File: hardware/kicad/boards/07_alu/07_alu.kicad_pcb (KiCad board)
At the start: 2 copper layers, 99.8 x 99.7 mm, 185 parts, among them J10 Conn_01x04_Pin, J11 Conn_01x04_Pin, J12 Conn_01x08_Pin, J15 Conn_01x08_Pin, J16 Conn_01x08_Pin, J17 Conn_01x08_Pin, J5 Conn_01x08_Pin, J6 Conn_01x08_Pin, J7 Conn_01x08_Pin, U16 74ACT151, U3 74ACT283, U36 74HC86, U37 74LS08, U38 74LS540, U4 74HC688, U40 74LS377, U41 74ACT151, U42 74ACT151, U43 74ACT151, U44 74ACT151, U45 74ACT151, U46 74ACT151, U47 74ACT151, U48 74ACT151, U49 74ACT151, U5 74ACT283, U50 74ACT151, U51 74ACT151, U52 74ACT151, U53 74ACT151, U54 74ACT151, U55 74ACT151, U56 74ACT151

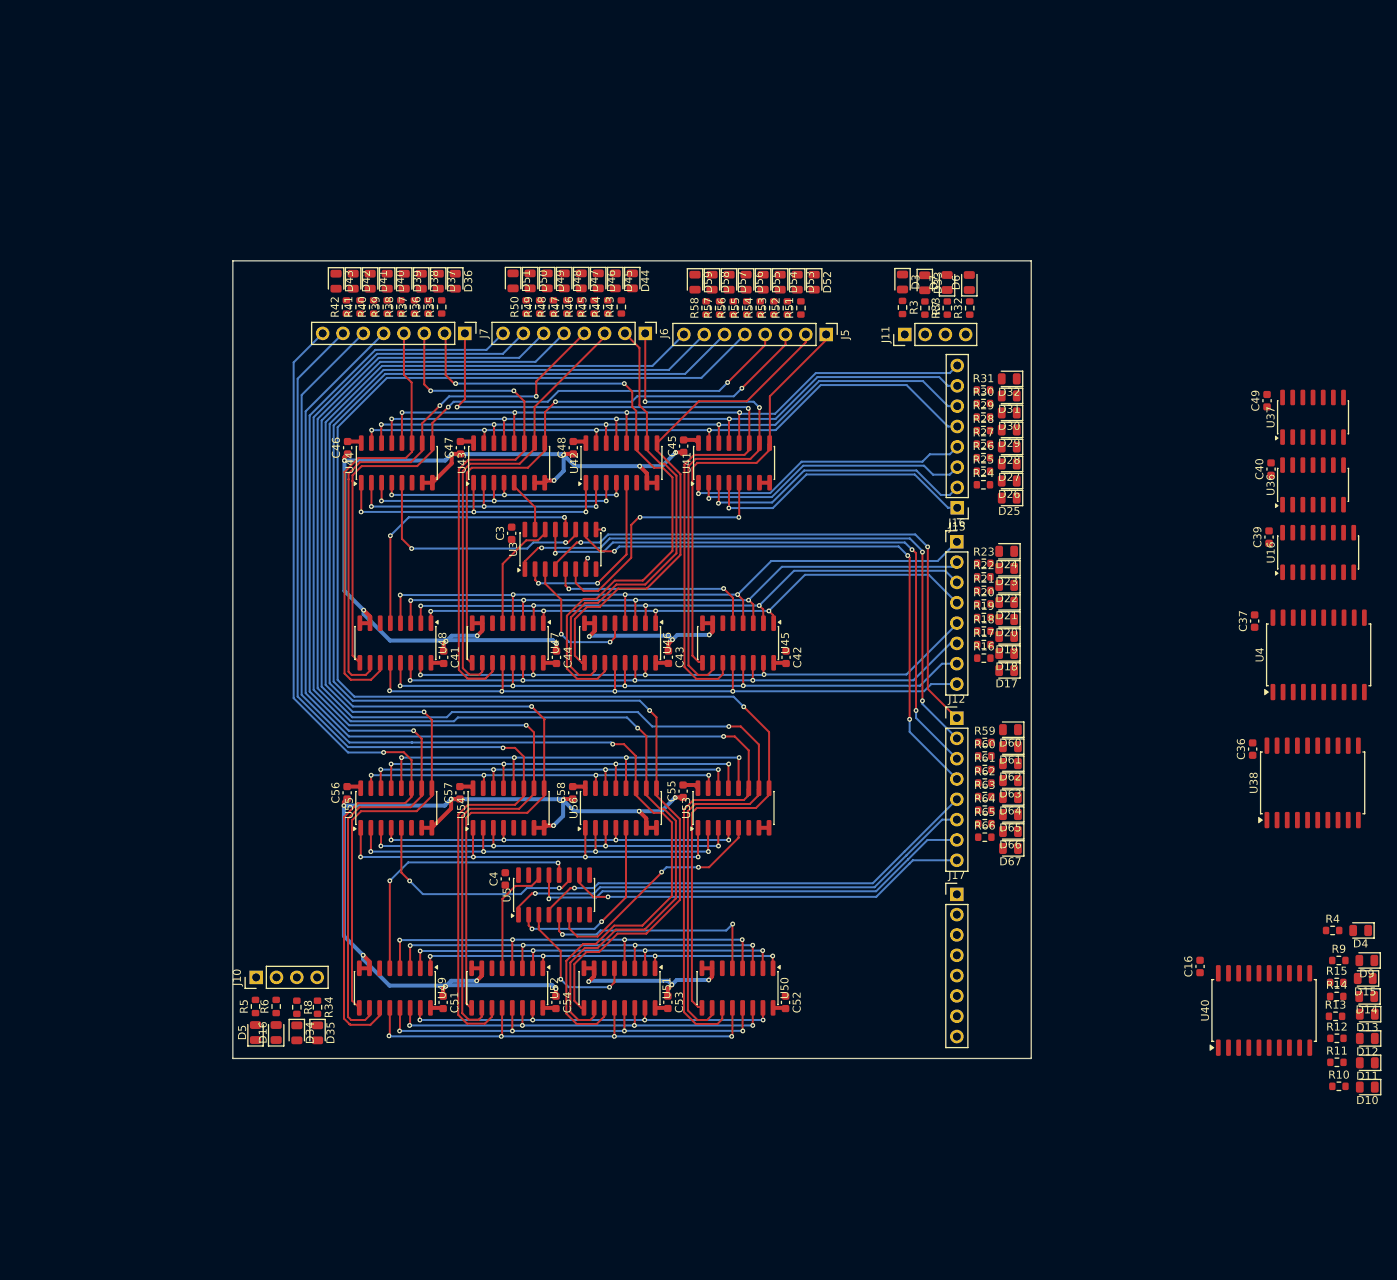
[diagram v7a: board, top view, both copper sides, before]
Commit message: checkpoint: routing flags and finishing final traces before pcb annotations and text
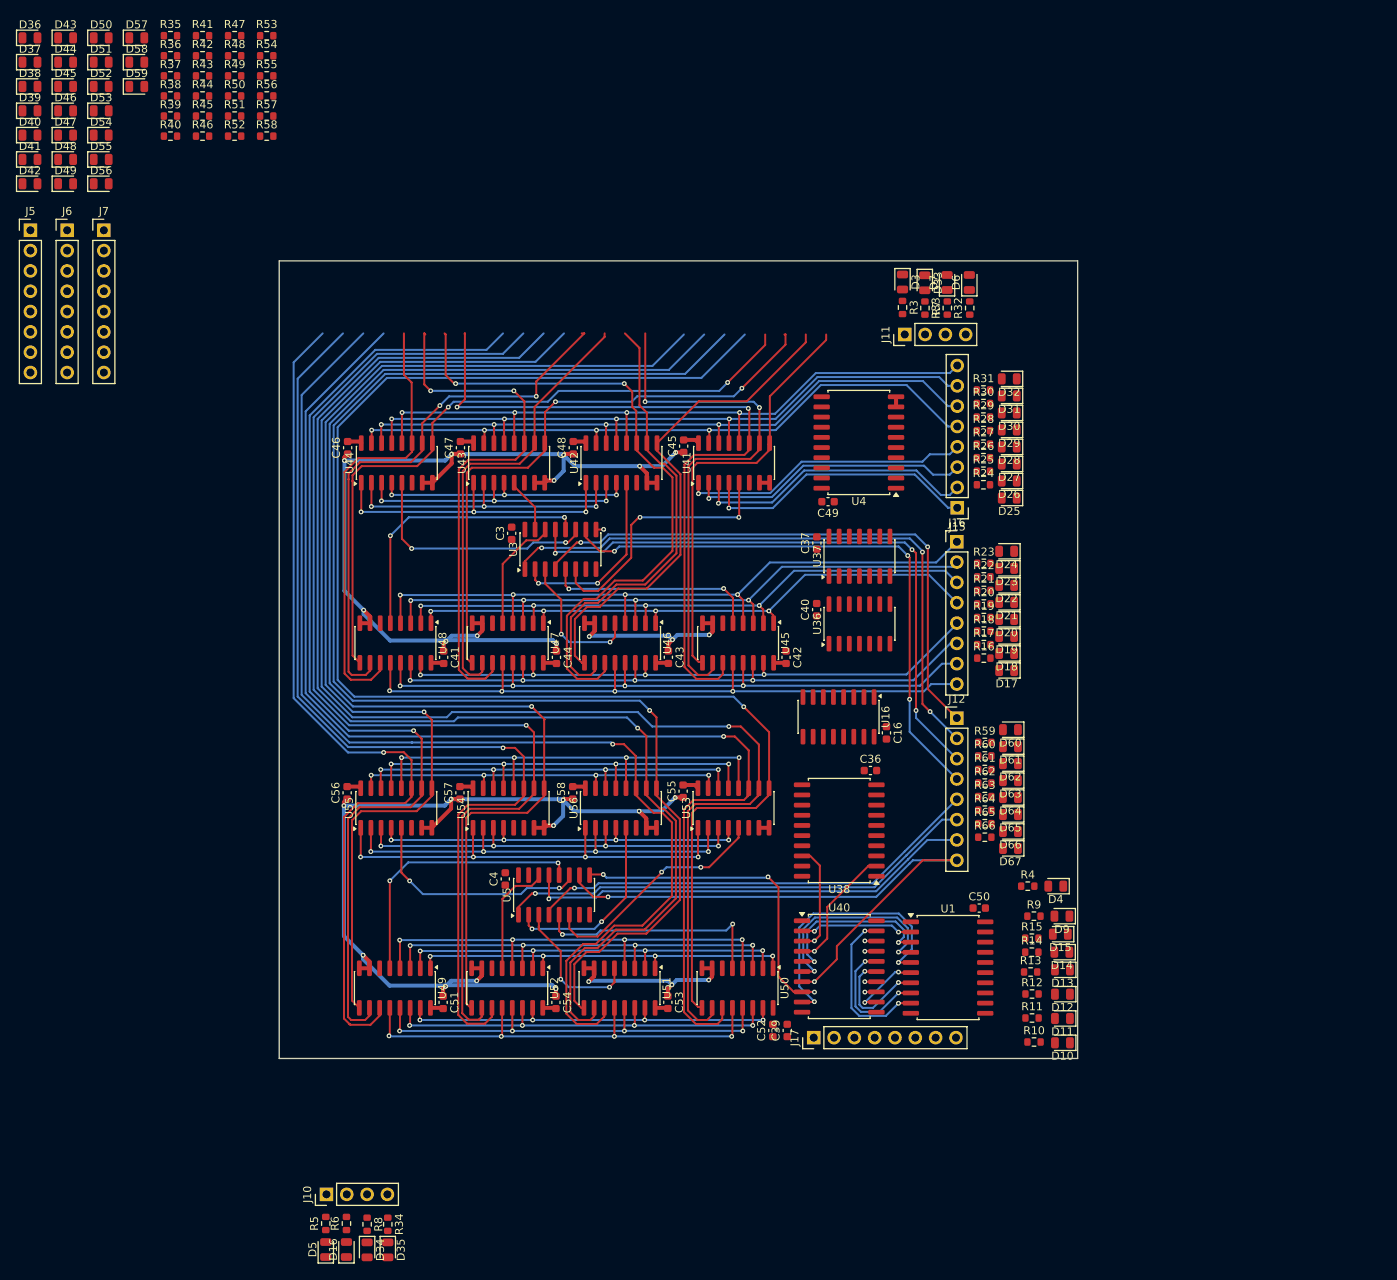
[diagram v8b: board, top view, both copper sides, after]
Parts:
- added C50: 100nF, Capacitor_SMD:C_0603_1608Metric, F.Cu at (149.7, 124.2)
- added U1: 74AHC541, Package_SO:SOIC-20W_7.5x12.8mm_P1.27mm, F.Cu at (145.8, 131.6)
- moved J5 100.3 mm to (31.1, 39.5), turned to 0 degrees
- moved D52 92.4 mm to (39.9, 21.5), turned to 0 degrees
- moved D53 89.6 mm to (39.9, 24.5), turned to 0 degrees
- moved D54 86.8 mm to (39.9, 27.6), turned to 0 degrees
- moved C39 86.2 mm to (125.7, 139.5)
- moved D55 84.1 mm to (39.9, 30.6), turned to 0 degrees
- moved D56 81.5 mm to (39.9, 33.7), turned to 0 degrees
- moved D57 80.1 mm to (44.4, 15.4), turned to 0 degrees
- moved D58 77.0 mm to (44.4, 18.5), turned to 0 degrees
- moved D44 75.9 mm to (35.5, 18.5), turned to 0 degrees
- moved R51 74.7 mm to (56.6, 25.2), turned to 0 degrees
- moved D59 73.9 mm to (44.4, 21.5), turned to 0 degrees
- moved J6 73.4 mm to (35.7, 39.5), turned to 0 degrees
- moved D45 72.9 mm to (35.5, 21.5), turned to 0 degrees
- moved R52 72.4 mm to (56.6, 27.7), turned to 0 degrees
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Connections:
- J17 pad 1: CSEL0 -> CSEL2
- J17 pad 3: CSEL2 -> CSEL0
- U40 pad 12: flagV -> Net-(U1-A4)
- U40 pad 15: flagLT -> Net-(U1-A5)
- U40 pad 16: flagGT -> Net-(U1-A6)
- U40 pad 19: flagGTE -> Net-(U1-A7)
- U40 pad 2: flagZ -> Net-(U1-A0)
- U40 pad 5: ~flagZ -> Net-(U1-A1)
- U40 pad 6: flagN -> Net-(U1-A2)
- U40 pad 9: flagC -> Net-(U1-A3)
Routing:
- net COUT-MAIN: track 0.00 -> 40.8 mm, vias 0 -> 3
- net Net-(U1-A3): track 0.00 -> 33.8 mm, vias 0 -> 2
- net Net-(U1-A2): track 0.00 -> 26.7 mm, vias 0 -> 2
- net OUT7: track 50.8 -> 77.4 mm, vias 1 -> 2
- net Net-(U1-A1): track 0.00 -> 22.2 mm, vias 0 -> 2
- net Net-(U1-A7): track 0.00 -> 20.3 mm, vias 0 -> 2
- net ~ZOUT: track 0.00 -> 16.0 mm, vias 0 -> 1
- net Net-(U1-A6): track 0.00 -> 15.7 mm, vias 0 -> 2
- net Net-(U1-A0): track 0.00 -> 14.3 mm, vias 0 -> 2
- net ZOUT: track 0.00 -> 14.0 mm, vias 0 -> 1
- net Net-(U1-A5): track 0.00 -> 13.8 mm, vias 0 -> 2
- net Net-(U1-A4): track 0.00 -> 8.83 mm, vias 0 -> 2
- net CIN-MAIN: track 1.69 -> 0.00 mm, vias 1 -> 0
- net VCC: track 27.4 -> 25.8 mm
- net VOUT: track 0.00 -> 1.46 mm, vias 0 -> 1
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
